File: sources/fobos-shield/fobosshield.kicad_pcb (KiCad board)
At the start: 2 copper layers, 83.8 x 63.5 mm, 154 parts, among them J1 Target, J10 ADCin, J11 PP1, J12 PP2, J13 Clock, J14 Trigger, J15 CSM5VCur, J16 Conn_01x01, J17 Barrel_Jack_Switch, J18 Conn_01x02, J19 Conn_01x02, J2 Glitch, J20 CSM3V3Cur, J21 GND, J22 GND, J3 Analog, J4 IOH, J5 SPI, J6 Analog2, J7 Power, J8 IOL, J9 SPI2, Q1 IRF7807Z, Q2 IRLML2502, Q3 BSS138L, U1 RB-0509D, U10 INA225, U11 INA225, U12 LD1117S33TR_SOT223, U2 REE-0505S, U3 LM317L_SO8, U4 LM337L_SO8, U5 LD59015, U6 LD3985G33R_TSOT23, U7 AD8331, U8 TPS7A7100_VQFN20, U9 AD9215

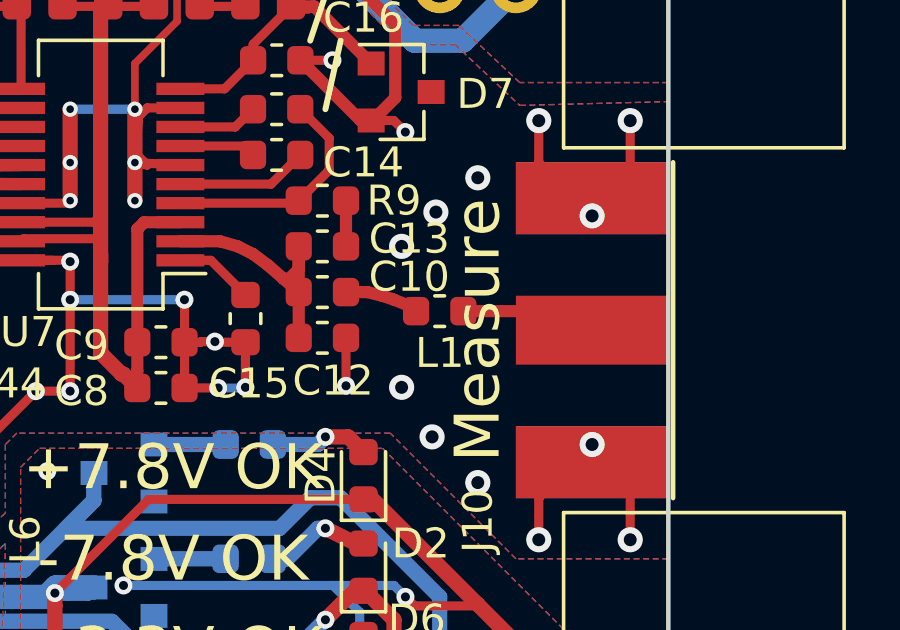
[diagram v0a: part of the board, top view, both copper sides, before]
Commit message: inductor size changed
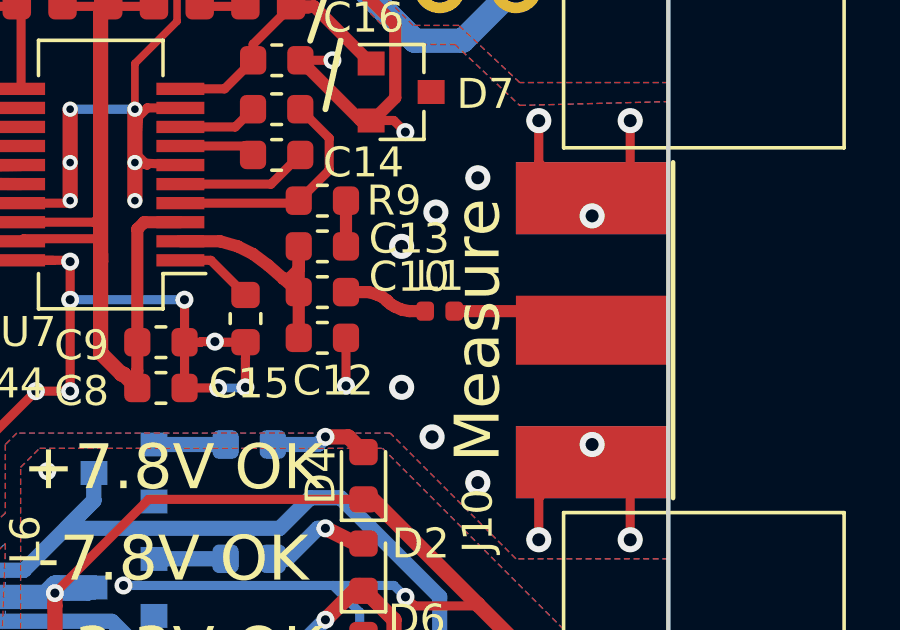
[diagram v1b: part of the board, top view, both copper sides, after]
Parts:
- L1: footprint Inductor_SMD:L_0603_1608Metric -> Inductor_SMD:L_0402_1005Metric
- L5: value L_Core_Ferrite -> 1k/500mA
- R12, R13: value 2k2 -> 2k
- R18: value 1k -> 100R
- U6: value LD3985G33R_TSOT23 -> LP3985IM5-3.0
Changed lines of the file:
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@@
     (thickness 1.6002)
     (drawings 62)
-    (tracks 1847)
+    (tracks 1853)
     (zones 0)
     (modules 154)
@@
   )
   (setup
-    (last_trace_width 0.8128)
+    (last_trace_width 0.4064)
     (user_trace_width 0.254)
     (user_trace_width 0.3048)
@@
     (add_net XADC_V_P)
   )
+  (module Inductor_SMD:L_0402_1005Metric (layer F.Cu)
+    (at 113.03 62.865)
+    (descr "Inductor SMD 0402 (1005 Metric), square (rectangular) end terminal, IPC_7351 nominal, (Body size source: http://www.tortai-tech.com/upload/download/2011102023233369053.pdf), generated with kicad-footprint-generator")
+    (tags inductor)
+    (attr smd)
+    (fp_text reference L1 (at 0 -1.17) (layer F.SilkS)
+      (effects (font (size 1 1) (thickness 0.15)))
+    )
+    (fp_text value 120nH (at 0 1.17) (layer F.Fab)
+      (effects (font (size 1 1) (thickness 0.15)))
+    )
+    (fp_line (start -0.5 0.25) (end -0.5 -0.25) (layer F.Fab) (width 0.1))
+    (fp_line (start -0.5 -0.25) (end 0.5 -0.25) (layer F.Fab) (width 0.1))
+    (fp_line (start 0.5 -0.25) (end 0.5 0.25) (layer F.Fab) (width 0.1))
+    (fp_line (start 0.5 0.25) (end -0.5 0.25) (layer F.Fab) (width 0.1))
+    (fp_line (start -0.93 0.47) (end -0.93 -0.47) (layer F.CrtYd) (width 0.05))
+    (fp_line (start -0.93 -0.47) (end 0.93 -0.47) (layer F.CrtYd) (width 0.05))
+    (fp_line (start 0.93 -0.47) (end 0.93 0.47) (layer F.CrtYd) (width 0.05))
+    (fp_line (start 0.93 0.47) (end -0.93 0.47) (layer F.CrtYd) (width 0.05))
+    (fp_text user %R (at 0 0) (layer F.Fab)
+      (effects (font (size 0.25 0.25) (thickness 0.04)))
+    )
+    (pad 1 smd roundrect (at -0.485 0) (size 0.59 0.64) (layers F.Cu F.Paste F.Mask) (roundrect_rratio 0.25)
+      (net 33 "Net-(C10-Pad2)"))
+    (pad 2 smd roundrect (at 0.485 0) (size 0.59 0.64) (layers F.Cu F.Paste F.Mask) (roundrect_rratio 0.25)
+      (net 43 "Net-(J10-Pad1)"))
+    (model ${KISYS3DMOD}/Inductor_SMD.3dshapes/L_0402_1005Metric.wrl
+      (at (xyz 0 0 0))
+      (scale (xyz 1 1 1))
+      (rotate (xyz 0 0 0))
+    )
+  )
   (module Package_SO:SOIC-8_3.9x4.9mm_P1.27mm (layer F.Cu)
     (at 102.268 33.02)
@@
       (effects (font (size 1 1) (thickness 0.15)) (justify mirror))
     )
-    (fp_text value L_Core_Ferrite (at 0 -1.43 180) (layer B.Fab)
+    (fp_text value 1k/500mA (at 0 -1.43 180) (layer B.Fab)
       (effects (font (size 1 1) (thickness 0.15)) (justify mirror))
     )
@@
       (effects (font (size 1 1) (thickness 0.15)))
     )
-    (fp_text value 1k (at 0 1.43 180) (layer F.Fab)
+    (fp_text value 100R (at 0 1.43 180) (layer F.Fab)
       (effects (font (size 1 1) (thickness 0.15)))
     )
@@
       (effects (font (size 1 1) (thickness 0.15)))
     )
-    (fp_text value 2k2 (at 0 1.43 90) (layer F.Fab)
+    (fp_text value 2k (at 0 1.43 90) (layer F.Fab)
       (effects (font (size 1 1) (thickness 0.15)))
     )
@@
       (effects (font (size 1 1) (thickness 0.15)))
     )
-    (fp_text value 2k2 (at 0 1.43 90) (layer F.Fab)
+    (fp_text value 2k (at 0 1.43 90) (layer F.Fab)
       (effects (font (size 1 1) (thickness 0.15)))
     )
@@
   )
   (module Inductor_SMD:L_0603_1608Metric (layer F.Cu)
-    (at 113.03 62.865)
-    (descr "Inductor SMD 0603 (1608 Metric), square (rectangular) end terminal, IPC_7351 nominal, (Body size source: http://www.tortai-tech.com/upload/download/2011102023233369053.pdf), generated with kicad-footprint-generator")
-    (tags inductor)
-    (attr smd)
-    (fp_text reference L1 (at 0 1.397) (layer F.SilkS)
-      (effects (font (size 1 1) (thickness 0.15)))
-    )
-    (fp_text value 120nH (at 0 1.43) (layer F.Fab)
-      (effects (font (size 1 1) (thickness 0.15)))
-    )
-    (fp_line (start -0.8 0.4) (end -0.8 -0.4) (layer F.Fab) (width 0.1))
-    (fp_line (start -0.8 -0.4) (end 0.8 -0.4) (layer F.Fab) (width 0.1))
-    (fp_line (start 0.8 -0.4) (end 0.8 0.4) (layer F.Fab) (width 0.1))
-    (fp_line (start 0.8 0.4) (end -0.8 0.4) (layer F.Fab) (width 0.1))
-    (fp_line (start -0.162779 -0.51) (end 0.162779 -0.51) (layer F.SilkS) (width 0.12))
-    (fp_line (start -0.162779 0.51) (end 0.162779 0.51) (layer F.SilkS) (width 0.12))
-    (fp_line (start -1.48 0.73) (end -1.48 -0.73) (layer F.CrtYd) (width 0.05))
-    (fp_line (start -1.48 -0.73) (end 1.48 -0.73) (layer F.CrtYd) (width 0.05))
-    (fp_line (start 1.48 -0.73) (end 1.48 0.73) (layer F.CrtYd) (width 0.05))
-    (fp_line (start 1.48 0.73) (end -1.48 0.73) (layer F.CrtYd) (width 0.05))
-    (fp_text user %R (at 0 0) (layer F.Fab)
-      (effects (font (size 0.4 0.4) (thickness 0.06)))
-    )
-    (pad 1 smd roundrect (at -0.7875 0) (size 0.875 0.95) (layers F.Cu F.Paste F.Mask) (roundrect_rratio 0.25)
-      (net 33 "Net-(C10-Pad2)"))
-    (pad 2 smd roundrect (at 0.7875 0) (size 0.875 0.95) (layers F.Cu F.Paste F.Mask) (roundrect_rratio 0.25)
-      (net 43 "Net-(J10-Pad1)"))
-    (model ${KISYS3DMOD}/Inductor_SMD.3dshapes/L_0603_1608Metric.wrl
-      (at (xyz 0 0 0))
-      (scale (xyz 1 1 1))
-      (rotate (xyz 0 0 0))
-    )
-  )
-  (module Inductor_SMD:L_0603_1608Metric (layer F.Cu)
     (at 103.505 51.9175 90)
     (descr "Inductor SMD 0603 (1608 Metric), square (rectangular) end terminal, IPC_7351 nominal, (Body size source: http://www.tortai-tech.com/upload/download/2011102023233369053.pdf), generated with kicad-footprint-generator")
@@
       (effects (font (size 1 1) (thickness 0.15)))
     )
-    (fp_text value LD3985G33R_TSOT23 (at 0 2.5 90) (layer F.Fab)
+    (fp_text value LP3985IM5-3.0 (at 0 2.5 90) (layer F.Fab)
       (effects (font (size 1 1) (thickness 0.15)))
     )
@@
   (segment (start 99.07677 55.455652) (end 99.07677 52.84877) (width 0.3048) (layer F.Cu) (net 32))
   (segment (start 98.933 52.705) (end 97.409 52.705) (width 0.3048) (layer F.Cu) (net 32))
-  (segment (start 109.906 62.23) (end 110.617 62.23) (width 0.4064) (layer F.Cu) (net 33))
-  (segment (start 110.617 62.23) (end 111.125 62.357) (width 0.4064) (layer F.Cu) (net 33))
-  (segment (start 111.125 62.357) (end 111.506 62.484) (width 0.4064) (layer F.Cu) (net 33))
-  (segment (start 111.506 62.484) (end 112.141 62.738) (width 0.4064) (layer F.Cu) (net 33))
+  (segment (start 112.014 62.865) (end 112.395 62.865) (width 0.4064) (layer F.Cu) (net 33))
+  (segment (start 111.76 62.8142) (end 112.014 62.865) (width 0.4064) (layer F.Cu) (net 33))
+  (segment (start 111.5314 62.7126) (end 111.76 62.8142) (width 0.4064) (layer F.Cu) (net 33))
+  (segment (start 111.4044 62.6364) (end 111.5314 62.7126) (width 0.4064) (layer F.Cu) (net 33))
+  (segment (start 111.2774 62.5094) (end 111.252 62.5094) (width 0.4064) (layer F.Cu) (net 33))
+  (segment (start 110.6678 62.23) (end 110.9218 62.3062) (width 0.4064) (layer F.Cu) (net 33))
+  (segment (start 110.9218 62.3062) (end 111.0996 62.3824) (width 0.4064) (layer F.Cu) (net 33))
+  (segment (start 111.252 62.5094) (end 111.4044 62.6364) (width 0.4064) (layer F.Cu) (net 33))
+  (segment (start 109.906 62.23) (end 110.6678 62.23) (width 0.4064) (layer F.Cu) (net 33))
+  (segment (start 111.0996 62.3824) (end 111.2774 62.5094) (width 0.4064) (layer F.Cu) (net 33))
   (segment (start 96.52 58.674) (end 96.4185 58.674) (width 0.4064) (layer F.Cu) (net 34))
   (segment (start 96.774 58.5724) (end 96.52 58.674) (width 0.4064) (layer F.Cu) (net 34))
@@
   (segment (start 108.077 52.705) (end 108.839 52.705) (width 0.4064) (layer F.Cu) (net 42))
   (segment (start 117.475 62.865) (end 118.11 63.5) (width 0.4064) (layer F.Cu) (net 43))
-  (segment (start 113.8175 62.865) (end 116.84 62.865) (width 0.4064) (layer F.Cu) (net 43))
+  (segment (start 113.538 62.865) (end 116.84 62.865) (width 0.4064) (layer F.Cu) (net 43))
   (segment (start 90.17 31.115) (end 90.17 25.4) (width 0.508) (layer F.Cu) (net 44))
   (segment (start 89.535 31.75) (end 90.17 31.115) (width 0.508) (layer F.Cu) (net 44))

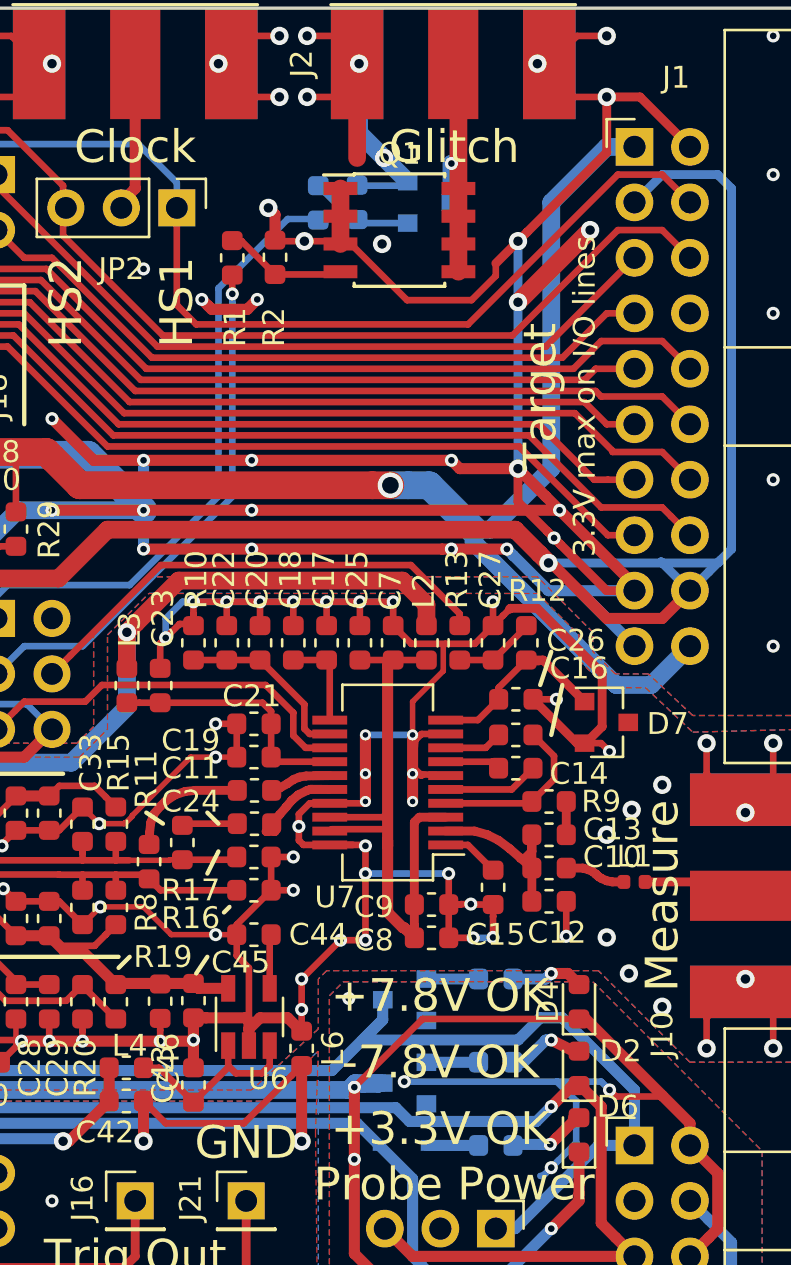
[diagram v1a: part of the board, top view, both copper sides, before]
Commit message: added CERG logo
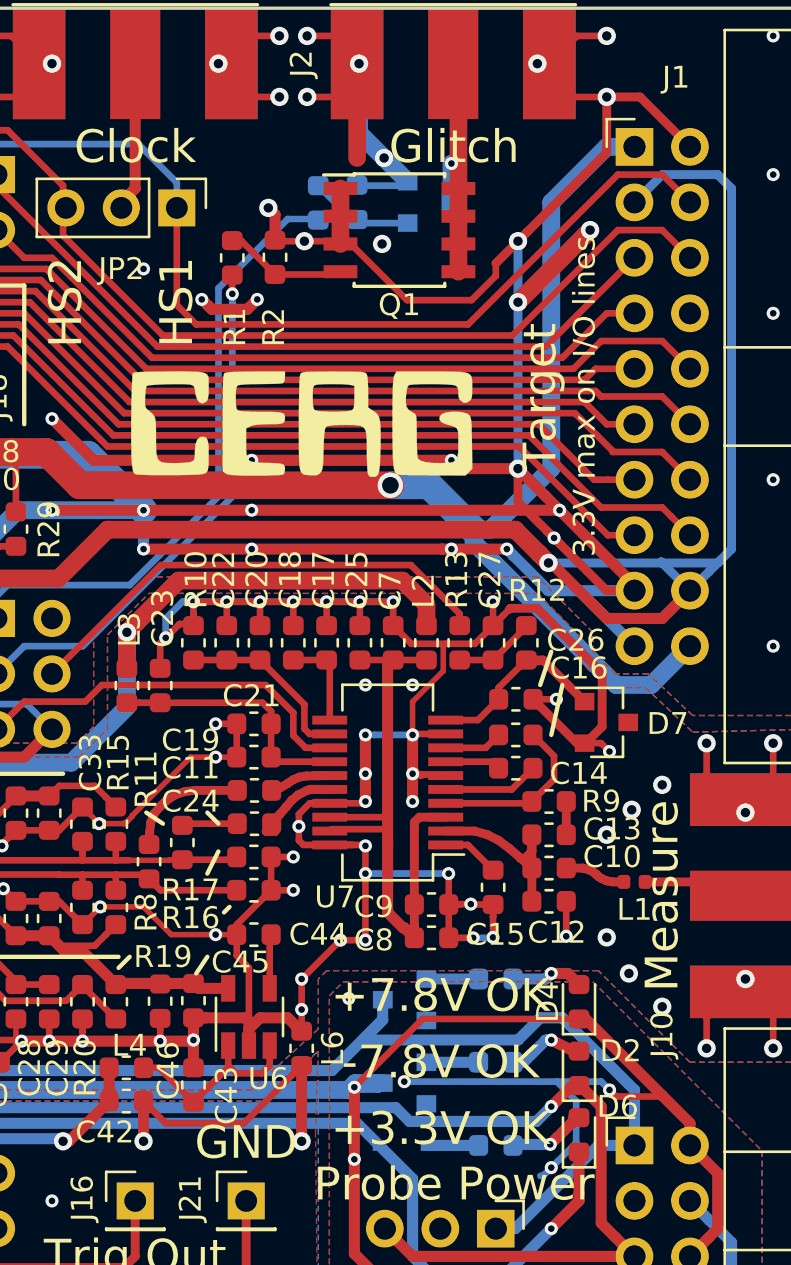
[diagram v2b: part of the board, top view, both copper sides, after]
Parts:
- added G***: LOGO, cerg:cerg, F.Cu at (97.8, 41.9)
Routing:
- net GNDA: track 230.5 -> 231.0 mm, vias 64 -> 66

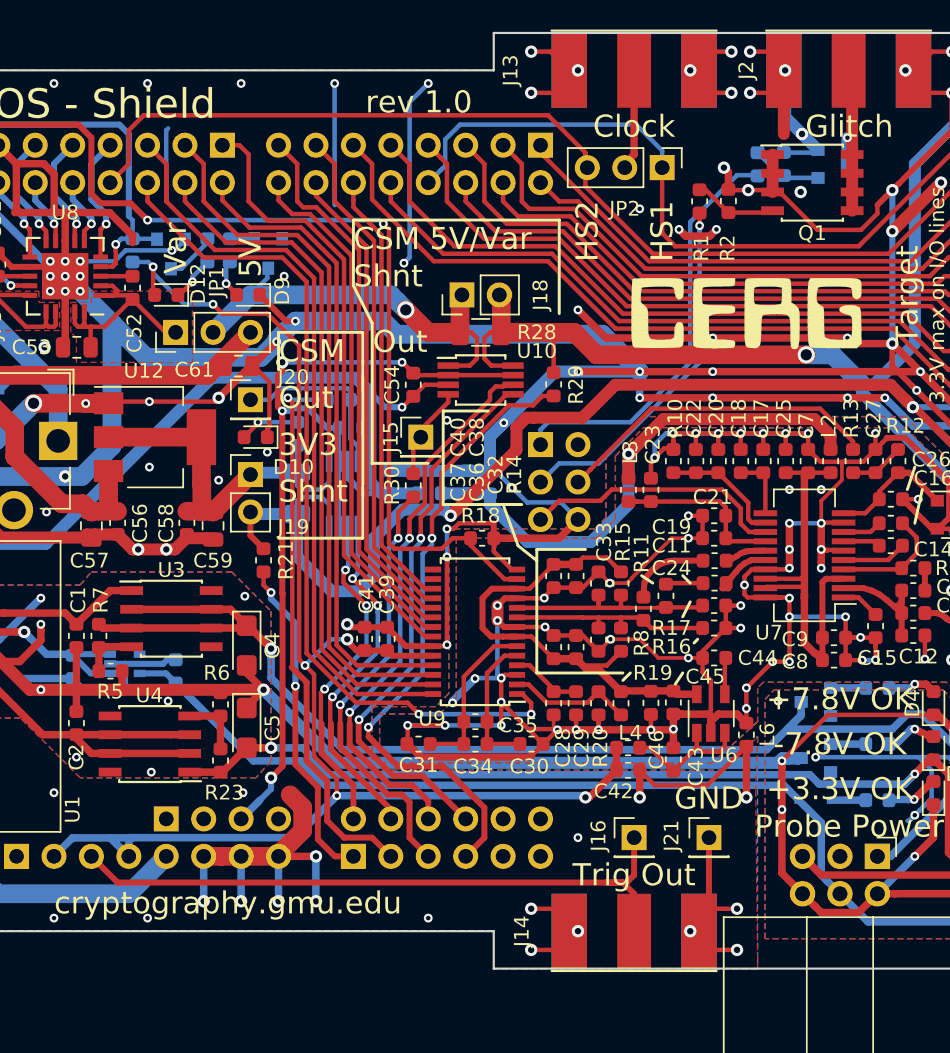
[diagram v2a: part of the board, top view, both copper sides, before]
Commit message: added FPGA pinouts and fixed 2 bugs
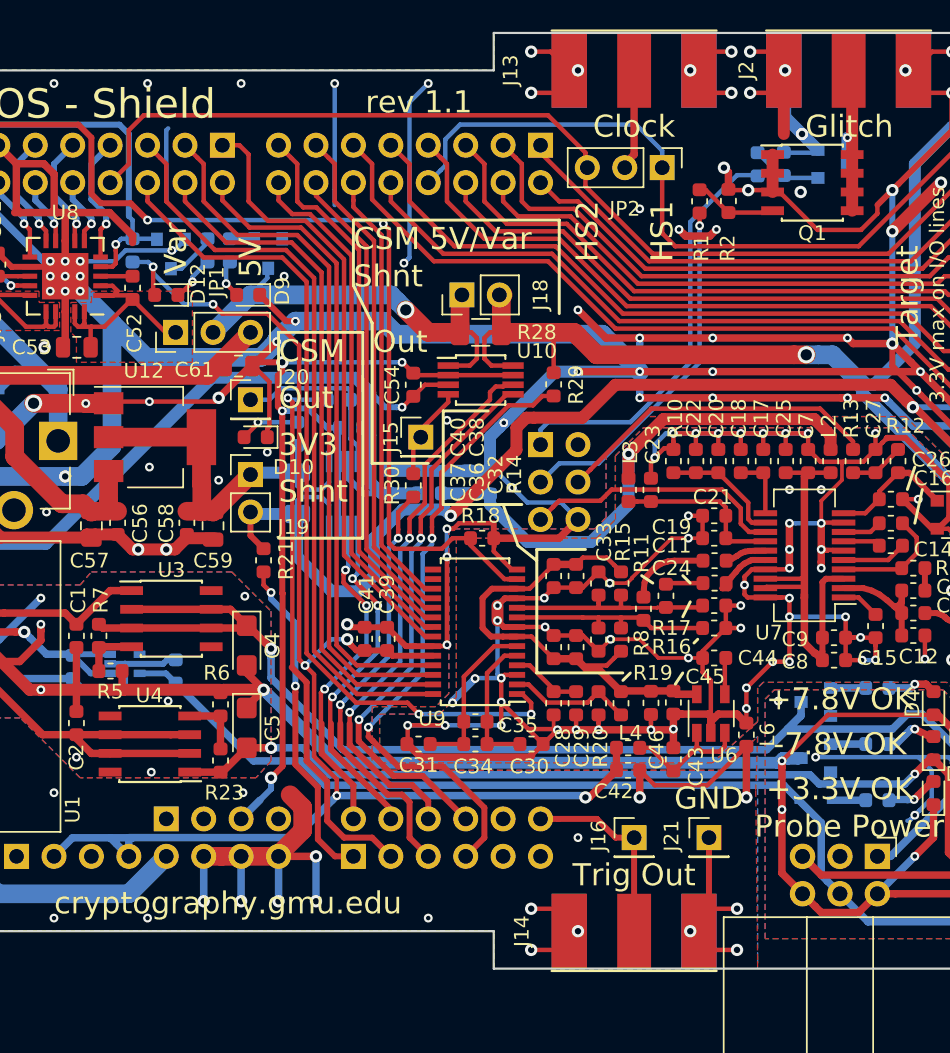
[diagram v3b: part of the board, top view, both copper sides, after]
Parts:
- removed G***: LOGO, cerg:cerg
- C1, C2: value 100nF -> 100n
- C51: value 10nF -> 10n
- C53: value 10uF X5R -> 10uF
- L2: value 1k500mA -> 1k/500mA
- R21, R29, R30, R31: value 1k68 1% -> 1k69 1%
- R7: value 240R,1% -> 240R, 1%
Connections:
- C54 pad 2: XADCGND -> GND
- C55 pad 2: XADCGND -> GND
- J3 pad 12: A11 -> Trigger
- J6 pad 3: XADCGND -> GND
- J7 pad 3: Trigger -> Net-(J7-Pad3)
- U10 pad 2: XADCGND -> GND
- U10 pad 7: XADCGND -> GND
- U11 pad 2: XADCGND -> GND
- U11 pad 7: XADCGND -> GND
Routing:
- net GND: track 499.5 -> 561.3 mm, vias 114 -> 118
- net XADCGND: track 59.6 -> 0.00 mm, vias 4 -> 0
- net Trigger: track 47.1 -> 13.2 mm
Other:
- board text added: "rev 1.1"
- board text removed: "rev 1.0"
